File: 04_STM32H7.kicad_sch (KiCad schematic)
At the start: 13 parts, among them U3 STM32H743ZIT6, U4 REF3033

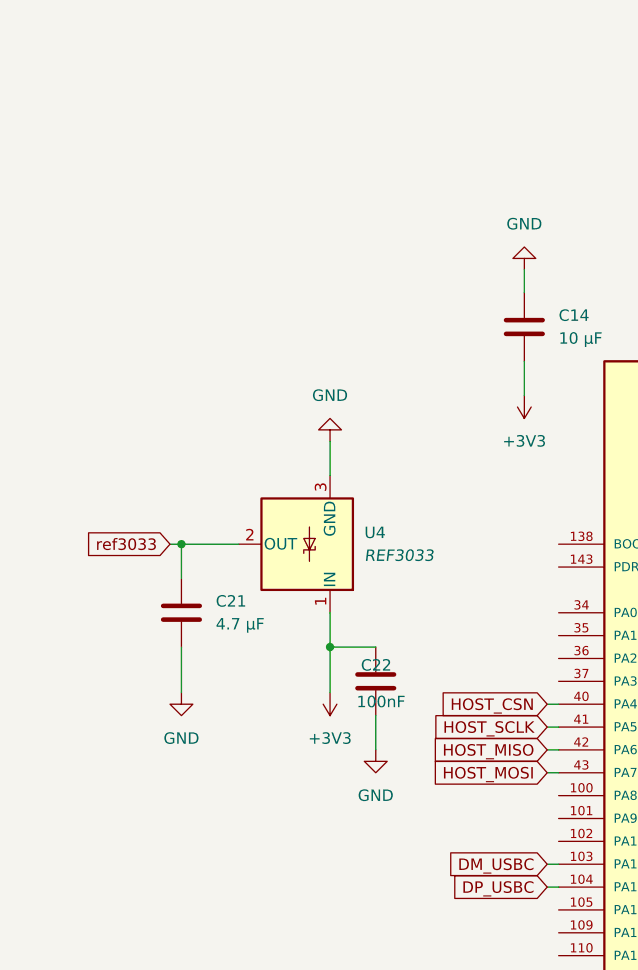
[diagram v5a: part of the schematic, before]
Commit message: added user ports
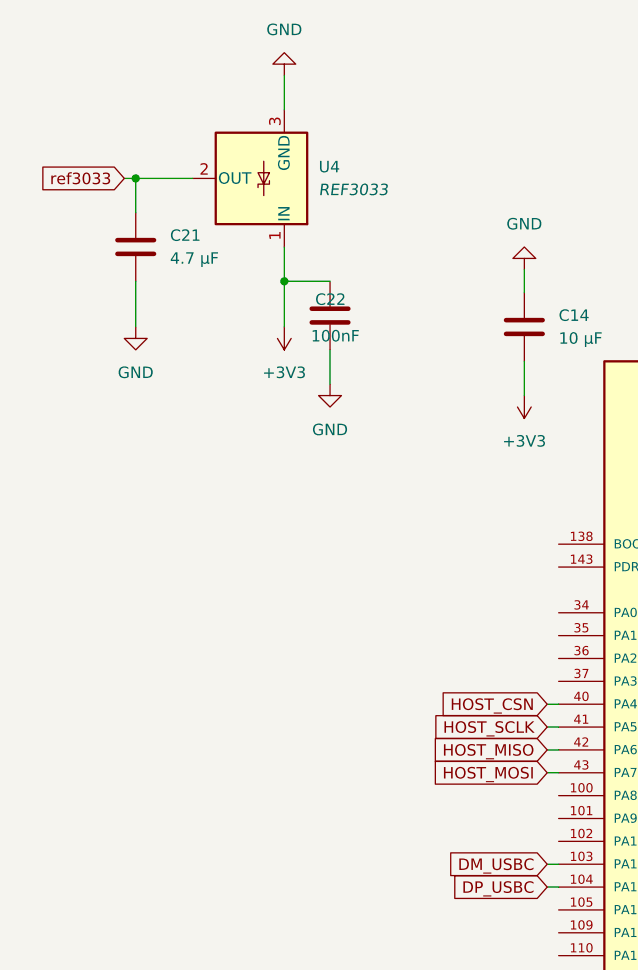
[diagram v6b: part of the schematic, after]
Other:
- moved on the sheet: C21, C22, U4
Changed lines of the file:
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@@
 	)
 	(junction
-		(at 52.07 86.36)
+		(at 46.99 45.72)
 		(diameter 0)
 		(color 0 0 0 0)
@@
 	)
 	(junction
-		(at 35.56 74.93)
+		(at 30.48 34.29)
 		(diameter 0)
 		(color 0 0 0 0)
@@
 	(wire
 		(pts
-			(xy 52.07 86.36) (xy 52.07 91.44)
+			(xy 46.99 45.72) (xy 46.99 50.8)
 		)
 		(stroke
@@
 	(wire
 		(pts
-			(xy 57.15 93.98) (xy 57.15 97.79)
+			(xy 52.07 53.34) (xy 52.07 57.15)
 		)
 		(stroke
@@
 	(wire
 		(pts
-			(xy 35.56 74.93) (xy 41.91 74.93)
+			(xy 30.48 34.29) (xy 36.83 34.29)
 		)
 		(stroke
@@
 	(wire
 		(pts
-			(xy 52.07 82.55) (xy 52.07 86.36)
+			(xy 46.99 41.91) (xy 46.99 45.72)
 		)
 		(stroke
@@
 	(wire
 		(pts
-			(xy 35.56 74.93) (xy 35.56 78.74)
+			(xy 30.48 34.29) (xy 30.48 38.1)
 		)
 		(stroke
@@
 	(wire
 		(pts
-			(xy 35.56 86.36) (xy 35.56 91.44)
+			(xy 30.48 45.72) (xy 30.48 50.8)
 		)
 		(stroke
@@
 	(wire
 		(pts
-			(xy 52.07 63.5) (xy 52.07 67.31)
+			(xy 46.99 22.86) (xy 46.99 26.67)
 		)
 		(stroke
@@
 	(wire
 		(pts
-			(xy 52.07 86.36) (xy 57.15 86.36)
+			(xy 46.99 45.72) (xy 52.07 45.72)
 		)
 		(stroke
@@
 	(wire
 		(pts
-			(xy 34.29 74.93) (xy 35.56 74.93)
+			(xy 29.21 34.29) (xy 30.48 34.29)
 		)
 		(stroke
@@
 	(global_label "ref3033"
 		(shape input)
-		(at 34.29 74.93 180)
+		(at 29.21 34.29 180)
 		(fields_autoplaced yes)
 		(effects
@@
 		)
 		(property "Intersheetrefs" "${INTERSHEET_REFS}"
-			(at 23.8663 74.93 0)
+			(at 18.7863 34.29 0)
 			(hide yes)
 			(show_name no)
@@
 	(symbol
 		(lib_id "power:+3V3")
-		(at 52.07 91.44 180)
+		(at 46.99 50.8 180)
 		(unit 1)
 		(body_style 1)
@@
 		(fields_autoplaced yes)
 		(property "Reference" "#PWR037"
-			(at 52.07 87.63 0)
+			(at 46.99 46.99 0)
 			(hide yes)
 			(show_name no)
@@
 		)
 		(property "Value" "+3V3"
-			(at 52.07 96.52 0)
+			(at 46.99 55.88 0)
 			(show_name no)
 			(do_not_autoplace no)
@@
 		)
 		(property "Footprint" ""
-			(at 52.07 91.44 0)
+			(at 46.99 50.8 0)
 			(hide yes)
 			(show_name no)
@@
 		)
 		(property "Datasheet" ""
-			(at 52.07 91.44 0)
+			(at 46.99 50.8 0)
 			(hide yes)
 			(show_name no)
@@
 		)
 		(property "Description" "Power symbol creates a global label with name \"+3V3\""
-			(at 52.07 91.44 0)
+			(at 46.99 50.8 0)
 			(hide yes)
 			(show_name no)
@@
 	(symbol
 		(lib_id "power:GND")
-		(at 52.07 63.5 180)
+		(at 46.99 22.86 180)
 		(unit 1)
 		(body_style 1)
@@
 		(fields_autoplaced yes)
 		(property "Reference" "#PWR040"
-			(at 52.07 57.15 0)
+			(at 46.99 16.51 0)
 			(hide yes)
 			(show_name no)
@@
 		)
 		(property "Value" "GND"
-			(at 52.07 58.42 0)
+			(at 46.99 17.78 0)
 			(show_name no)
 			(do_not_autoplace no)
@@
 		)
 		(property "Footprint" ""
-			(at 52.07 63.5 0)
+			(at 46.99 22.86 0)
 			(hide yes)
 			(show_name no)
@@
 		)
 		(property "Datasheet" ""
-			(at 52.07 63.5 0)
+			(at 46.99 22.86 0)
 			(hide yes)
 			(show_name no)
@@
 		)
 		(property "Description" "Power symbol creates a global label with name \"GND\" , ground"
-			(at 52.07 63.5 0)
+			(at 46.99 22.86 0)
 			(hide yes)
 			(show_name no)
@@
 	(symbol
 		(lib_id "power:GND")
-		(at 35.56 91.44 0)
+		(at 30.48 50.8 0)
 		(unit 1)
 		(body_style 1)
@@
 		(fields_autoplaced yes)
 		(property "Reference" "#PWR038"
-			(at 35.56 97.79 0)
+			(at 30.48 57.15 0)
 			(hide yes)
 			(show_name no)
@@
 		)
 		(property "Value" "GND"
-			(at 35.56 96.52 0)
+			(at 30.48 55.88 0)
 			(show_name no)
 			(do_not_autoplace no)
@@
 		)
 		(property "Footprint" ""
-			(at 35.56 91.44 0)
+			(at 30.48 50.8 0)
 			(hide yes)
 			(show_name no)
@@
 		)
 		(property "Datasheet" ""
-			(at 35.56 91.44 0)
+			(at 30.48 50.8 0)
 			(hide yes)
 			(show_name no)
@@
 		)
 		(property "Description" "Power symbol creates a global label with name \"GND\" , ground"
-			(at 35.56 91.44 0)
+			(at 30.48 50.8 0)
 			(hide yes)
 			(show_name no)
@@
 	(symbol
 		(lib_id "Reference_Voltage:REF3033")
-		(at 49.53 74.93 180)
+		(at 44.45 34.29 180)
 		(unit 1)
 		(body_style 1)
@@
 		(fields_autoplaced yes)
 		(property "Reference" "U4"
-			(at 55.88 73.6599 0)
+			(at 50.8 33.0199 0)
 			(show_name no)
 			(do_not_autoplace no)
@@
 		)
 		(property "Value" "REF3033"
-			(at 55.88 76.1999 0)
+			(at 50.8 35.5599 0)
 			(show_name no)
 			(do_not_autoplace no)
@@
 		)
 		(property "Footprint" "Package_TO_SOT_SMD:SOT-23"
-			(at 49.53 63.5 0)
+			(at 44.45 22.86 0)
 			(hide yes)
 			(show_name no)
@@
 		)
 		(property "Datasheet" "http://www.ti.com/lit/ds/symlink/ref3033.pdf"
-			(at 46.99 66.04 0)
+			(at 41.91 25.4 0)
 			(hide yes)
 			(show_name no)
@@
 		)
 		(property "Description" "3.3V 50-ppm/°C Max, 50-μA, CMOS Voltage Reference, SOT-23-3"
-			(at 49.53 74.93 0)
+			(at 44.45 34.29 0)
 			(hide yes)
 			(show_name no)
@@
 	(symbol
 		(lib_id "Device:C")
-		(at 35.56 82.55 0)
+		(at 30.48 41.91 0)
 		(unit 1)
 		(body_style 1)
@@
 		(fields_autoplaced yes)
 		(property "Reference" "C21"
-			(at 39.37 81.2799 0)
+			(at 34.29 40.6399 0)
 			(show_name no)
 			(do_not_autoplace no)
@@
 		)
 		(property "Value" "4.7 µF"
-			(at 39.37 83.8199 0)
+			(at 34.29 43.1799 0)
 			(show_name no)
 			(do_not_autoplace no)
@@
 		)
 		(property "Footprint" "Capacitor_SMD:C_0805_2012Metric_Pad1.18x1.45mm_HandSolder"
-			(at 36.5252 86.36 0)
+			(at 31.4452 45.72 0)
 			(hide yes)
 			(show_name no)
@@
 		)
 		(property "Datasheet" ""
-			(at 35.56 82.55 0)
+			(at 30.48 41.91 0)
 			(hide yes)
 			(show_name no)
@@
 		)
 		(property "Description" "Unpolarized capacitor"
-			(at 35.56 82.55 0)
+			(at 30.48 41.91 0)
 			(hide yes)
 			(show_name no)
@@
 	(symbol
 		(lib_id "power:GND")
-		(at 57.15 97.79 0)
+		(at 52.07 57.15 0)
 		(unit 1)
 		(body_style 1)
@@
 		(fields_autoplaced yes)
 		(property "Reference" "#PWR039"
-			(at 57.15 104.14 0)
+			(at 52.07 63.5 0)
 			(hide yes)
 			(show_name no)
@@
 		)
 		(property "Value" "GND"
-			(at 57.15 102.87 0)
+			(at 52.07 62.23 0)
 			(show_name no)
 			(do_not_autoplace no)
@@
 		)
 		(property "Footprint" ""
-			(at 57.15 97.79 0)
+			(at 52.07 57.15 0)
 			(hide yes)
 			(show_name no)
@@
 		)
 		(property "Datasheet" ""
-			(at 57.15 97.79 0)
+			(at 52.07 57.15 0)
 			(hide yes)
 			(show_name no)
@@
 		)
 		(property "Description" "Power symbol creates a global label with name \"GND\" , ground"
-			(at 57.15 97.79 0)
+			(at 52.07 57.15 0)
 			(hide yes)
 			(show_name no)
@@
 	(symbol
 		(lib_id "Device:C")
-		(at 57.15 90.17 180)
+		(at 52.07 49.53 180)
 		(unit 1)
 		(body_style 1)
@@
 		(dnp no)
 		(property "Reference" "C22"
-			(at 58.928 88.392 0)
+			(at 53.848 47.752 0)
 			(show_name no)
 			(do_not_autoplace no)
@@
 		)
 		(property "Value" "100nF"
-			(at 60.452 92.456 0)
+			(at 55.372 51.816 0)
 			(show_name no)
 			(do_not_autoplace no)
@@
 		)
 		(property "Footprint" "Capacitor_SMD:C_0805_2012Metric_Pad1.18x1.45mm_HandSolder"
-			(at 56.1848 86.36 0)
+			(at 51.1048 45.72 0)
 			(hide yes)
 			(show_name no)
@@
 		)
 		(property "Datasheet" ""
-			(at 57.15 90.17 0)
+			(at 52.07 49.53 0)
 			(hide yes)
 			(show_name no)
@@
 		)
 		(property "Description" "Unpolarized capacitor"
-			(at 57.15 90.17 0)
+			(at 52.07 49.53 0)
 			(hide yes)
 			(show_name no)

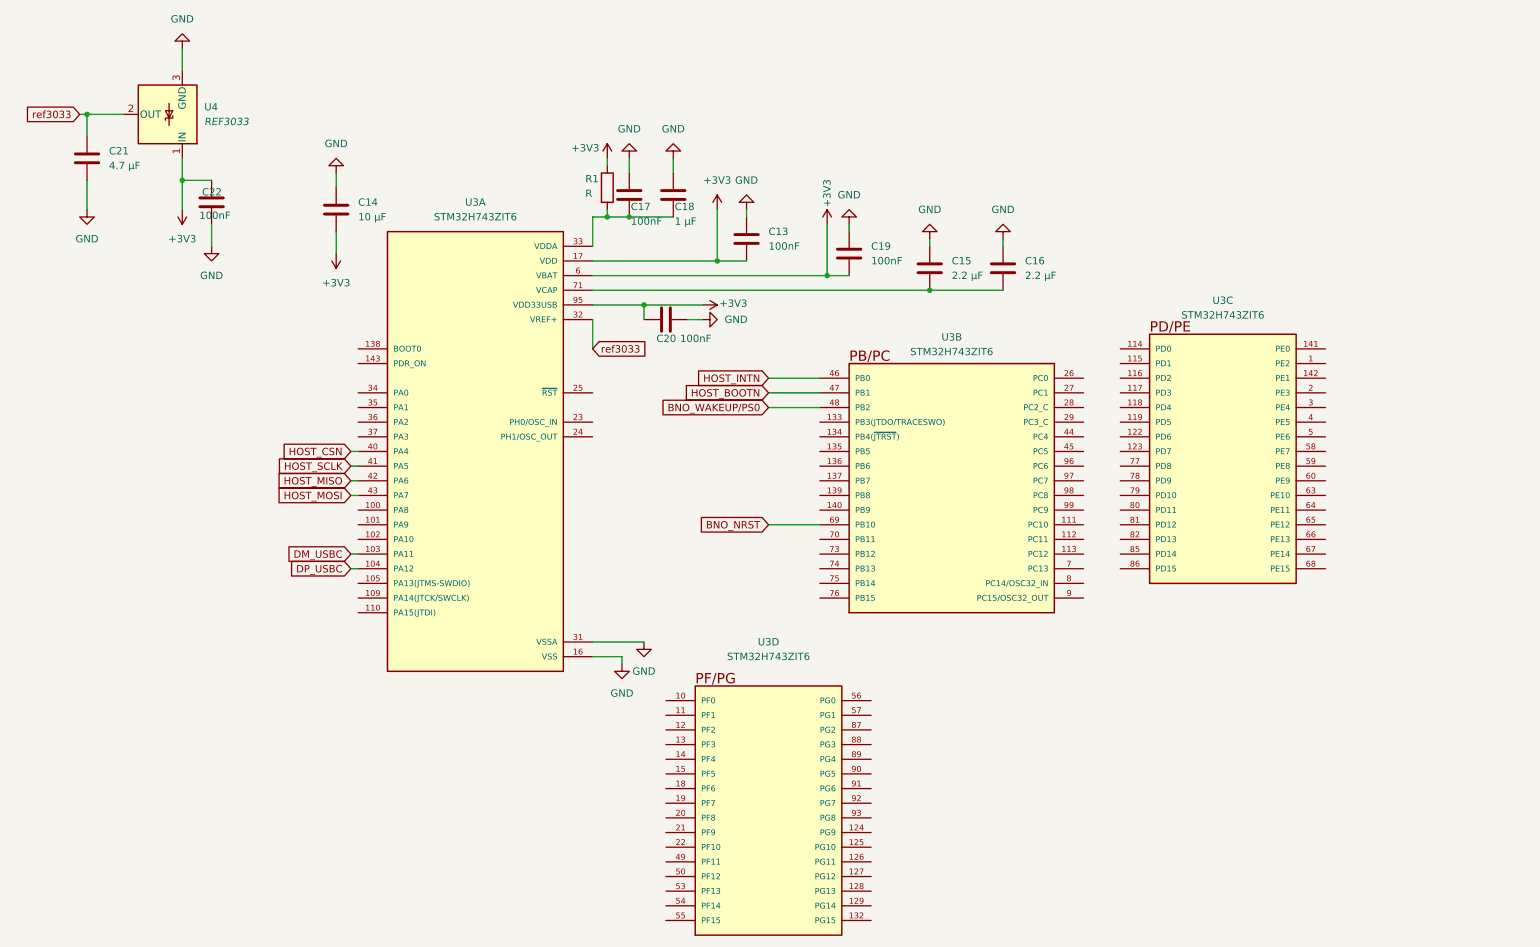
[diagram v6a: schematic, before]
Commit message: added mount vias and start placement uports
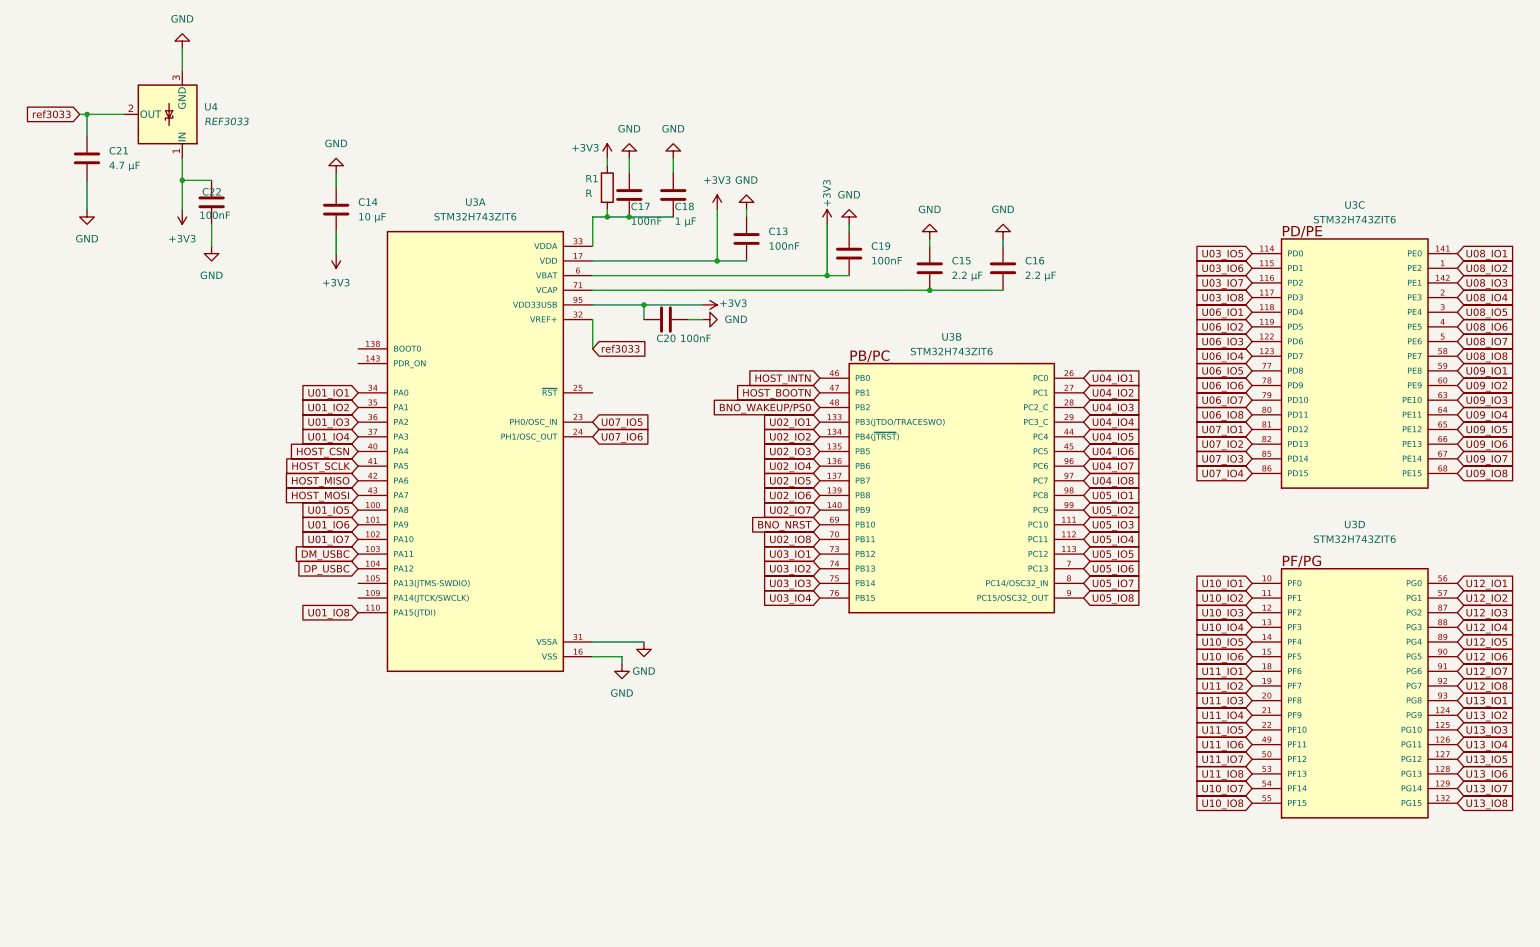
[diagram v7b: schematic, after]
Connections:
- net U01_IO5: now reaches U3.100 (PA8)
- net U01_IO6: now reaches U3.101 (PA9)
- net U01_IO7: now reaches U3.102 (PA10)
- net U01_IO8: now reaches U3.110 (PA15(JTDI))
- net U07_IO5: now reaches U3.23 (PH0/OSC_IN)
- net U07_IO6: now reaches U3.24 (PH1/OSC_OUT)
- net U01_IO1: now reaches U3.34 (PA0)
- net U01_IO2: now reaches U3.35 (PA1)
- net U01_IO3: now reaches U3.36 (PA2)
- net U01_IO4: now reaches U3.37 (PA3)
- net U05_IO3: now reaches U3.111 (PC10)
- net U05_IO4: now reaches U3.112 (PC11)
- net U05_IO5: now reaches U3.113 (PC12)
- net U02_IO1: now reaches U3.133 (PB3(JTDO/TRACESWO))
- net U02_IO2: now reaches U3.134 (PB4(~{JTRST}))
- net U02_IO3: now reaches U3.135 (PB5)
- net U02_IO4: now reaches U3.136 (PB6)
- net U02_IO5: now reaches U3.137 (PB7)
- net U02_IO6: now reaches U3.139 (PB8)
- net U02_IO7: now reaches U3.140 (PB9)
- net U04_IO1: now reaches U3.26 (PC0)
- net U04_IO2: now reaches U3.27 (PC1)
- net U04_IO3: now reaches U3.28 (PC2_C)
- net U04_IO4: now reaches U3.29 (PC3_C)
- net U04_IO5: now reaches U3.44 (PC4)
- net U04_IO6: now reaches U3.45 (PC5)
- net U05_IO6: now reaches U3.7 (PC13)
- net U02_IO8: now reaches U3.70 (PB11)
- net U03_IO1: now reaches U3.73 (PB12)
- net U03_IO2: now reaches U3.74 (PB13)
- net U03_IO3: now reaches U3.75 (PB14)
- net U03_IO4: now reaches U3.76 (PB15)
- net U05_IO7: now reaches U3.8 (PC14/OSC32_IN)
- net U05_IO8: now reaches U3.9 (PC15/OSC32_OUT)
- net U04_IO7: now reaches U3.96 (PC6)
- net U04_IO8: now reaches U3.97 (PC7)
- net U05_IO1: now reaches U3.98 (PC8)
- net U05_IO2: now reaches U3.99 (PC9)
- net U10_IO1: now reaches U3.10 (PF0)
- net U10_IO2: now reaches U3.11 (PF1)
- net U10_IO3: now reaches U3.12 (PF2)
- net U13_IO2: now reaches U3.124 (PG9)
- net U13_IO3: now reaches U3.125 (PG10)
- net U13_IO4: now reaches U3.126 (PG11)
- net U13_IO5: now reaches U3.127 (PG12)
- net U13_IO6: now reaches U3.128 (PG13)
- net U13_IO7: now reaches U3.129 (PG14)
- net U10_IO4: now reaches U3.13 (PF3)
- net U13_IO8: now reaches U3.132 (PG15)
- net U10_IO5: now reaches U3.14 (PF4)
- net U10_IO6: now reaches U3.15 (PF5)
- net U11_IO1: now reaches U3.18 (PF6)
- net U11_IO2: now reaches U3.19 (PF7)
- net U11_IO3: now reaches U3.20 (PF8)
- net U11_IO4: now reaches U3.21 (PF9)
- net U11_IO5: now reaches U3.22 (PF10)
- net U11_IO6: now reaches U3.49 (PF11)
- net U11_IO7: now reaches U3.50 (PF12)
- net U11_IO8: now reaches U3.53 (PF13)
- net U10_IO7: now reaches U3.54 (PF14)
- net U10_IO8: now reaches U3.55 (PF15)
- net U12_IO1: now reaches U3.56 (PG0)
- net U12_IO2: now reaches U3.57 (PG1)
- net U12_IO3: now reaches U3.87 (PG2)
- net U12_IO4: now reaches U3.88 (PG3)
- net U12_IO5: now reaches U3.89 (PG4)
- net U12_IO6: now reaches U3.90 (PG5)
- net U12_IO7: now reaches U3.91 (PG6)
- net U12_IO8: now reaches U3.92 (PG7)
- net U13_IO1: now reaches U3.93 (PG8)
- net U08_IO2: now reaches U3.1 (PE2)
- net U03_IO5: now reaches U3.114 (PD0)
- net U03_IO6: now reaches U3.115 (PD1)
- net U03_IO7: now reaches U3.116 (PD2)
- net U03_IO8: now reaches U3.117 (PD3)
- net U06_IO1: now reaches U3.118 (PD4)
- net U06_IO2: now reaches U3.119 (PD5)
- net U06_IO3: now reaches U3.122 (PD6)
- net U06_IO4: now reaches U3.123 (PD7)
- net U08_IO1: now reaches U3.141 (PE0)
- net U08_IO3: now reaches U3.142 (PE1)
- net U08_IO4: now reaches U3.2 (PE3)
- net U08_IO5: now reaches U3.3 (PE4)
- net U08_IO6: now reaches U3.4 (PE5)
- net U08_IO7: now reaches U3.5 (PE6)
- net U08_IO8: now reaches U3.58 (PE7)
- net U09_IO1: now reaches U3.59 (PE8)
- net U09_IO2: now reaches U3.60 (PE9)
- net U09_IO3: now reaches U3.63 (PE10)
- net U09_IO4: now reaches U3.64 (PE11)
- net U09_IO5: now reaches U3.65 (PE12)
- net U09_IO6: now reaches U3.66 (PE13)
- net U09_IO7: now reaches U3.67 (PE14)
- net U09_IO8: now reaches U3.68 (PE15)
- net U06_IO5: now reaches U3.77 (PD8)
- net U06_IO6: now reaches U3.78 (PD9)
- net U06_IO7: now reaches U3.79 (PD10)
- net U06_IO8: now reaches U3.80 (PD11)
- net U07_IO1: now reaches U3.81 (PD12)
- net U07_IO2: now reaches U3.82 (PD13)
- net U07_IO3: now reaches U3.85 (PD14)
- net U07_IO4: now reaches U3.86 (PD15)
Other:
- moved on the sheet: U3C, U3D

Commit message: added for 3v3 and 5v capacitors, resistors and induction footprints
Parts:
- C13, C17, C19, C20, C22: footprint Capacitor_SMD:C_0805_2012Metric_Pad1.18x1.45mm_HandSolder -> C1608X7R1H474K080AC:CAPC1608X90N
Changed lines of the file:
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@@
 			)
 		)
-		(property "Footprint" "Capacitor_SMD:C_0805_2012Metric_Pad1.18x1.45mm_HandSolder"
+		(property "Footprint" "C1608X7R1H474K080AC:CAPC1608X90N"
 			(at 163.5252 62.23 0)
 			(hide yes)
@@
 			)
 		)
-		(property "Footprint" "Capacitor_SMD:C_0805_2012Metric_Pad1.18x1.45mm_HandSolder"
+		(property "Footprint" "C1608X7R1H474K080AC:CAPC1608X90N"
 			(at 145.7452 59.69 0)
 			(hide yes)
@@
 			)
 		)
-		(property "Footprint" "Capacitor_SMD:C_0805_2012Metric_Pad1.18x1.45mm_HandSolder"
+		(property "Footprint" "C1608X7R1H474K080AC:CAPC1608X90N"
 			(at 125.4252 52.07 0)
 			(hide yes)
@@
 			)
 		)
-		(property "Footprint" "Capacitor_SMD:C_0805_2012Metric_Pad1.18x1.45mm_HandSolder"
+		(property "Footprint" "C1608X7R1H474K080AC:CAPC1608X90N"
 			(at 134.62 68.8848 0)
 			(hide yes)
@@
 			)
 		)
-		(property "Footprint" "Capacitor_SMD:C_0805_2012Metric_Pad1.18x1.45mm_HandSolder"
+		(property "Footprint" "C1608X7R1H474K080AC:CAPC1608X90N"
 			(at 51.1048 45.72 0)
 			(hide yes)
